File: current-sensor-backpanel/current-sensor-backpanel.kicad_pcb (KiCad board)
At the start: 2 copper layers, 98 x 30 mm, 6 parts

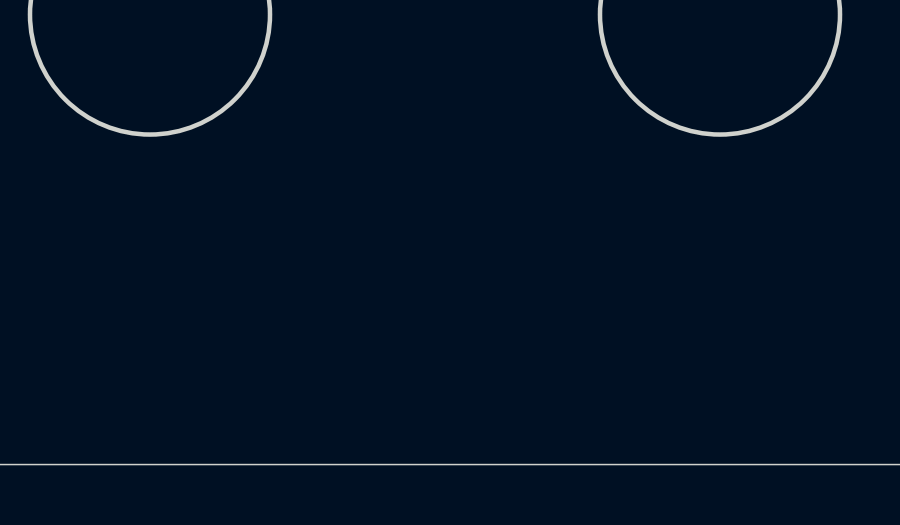
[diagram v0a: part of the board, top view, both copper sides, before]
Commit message: add JLC order number text to backpanel
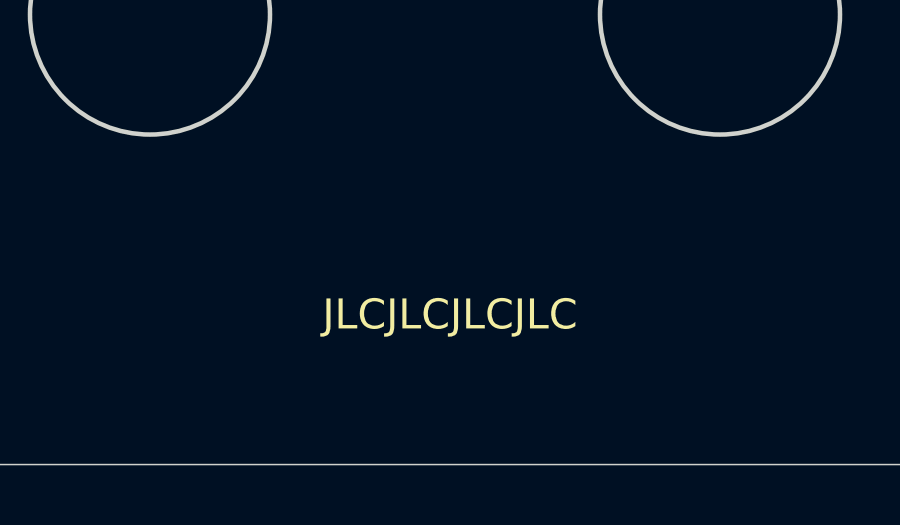
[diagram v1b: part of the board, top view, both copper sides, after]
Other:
- board text added: "JLCJLCJLCJLC"
